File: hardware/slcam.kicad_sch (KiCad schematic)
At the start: 33 parts, among them J1 532610671, J2 Conn_01x08, J3 Conn_01x04, J4 532610371, J5 532610371, U1 STM32F103C8Tx, U2 W25Q128JVS, U3 TCAN330G, U4 TPS2044D, Y1 Crystal_GND24

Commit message: hardware: Minor improvements in the schematics #28
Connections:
- no-connect marks 23 -> 30
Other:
- note added: "Boot options: BOOT0=0 BOOT1=x - Main flash memory boot BOOT0=1 BOOT1=0 - System memory boot (bootloader) BOOT0=1 BOOT1=1 - RAM memory"
- note added: "I2C Pull-Up"
- note added: "J4 - PicoBlade CAN - 3 pins"
- note removed: "Boot options: BOOT0=0 BOOT1=x - main flash memory boot BOOT0=1 BOOT1=0 - system memory boot (boot loader) BOOT0=1 BOOT1=1 - RAM memory"
- note removed: "J4 - Pico Blade CAN - 3 pins"
- note removed: "i2c Pull-up"
- moved on the sheet: R4, R5, R6, R7

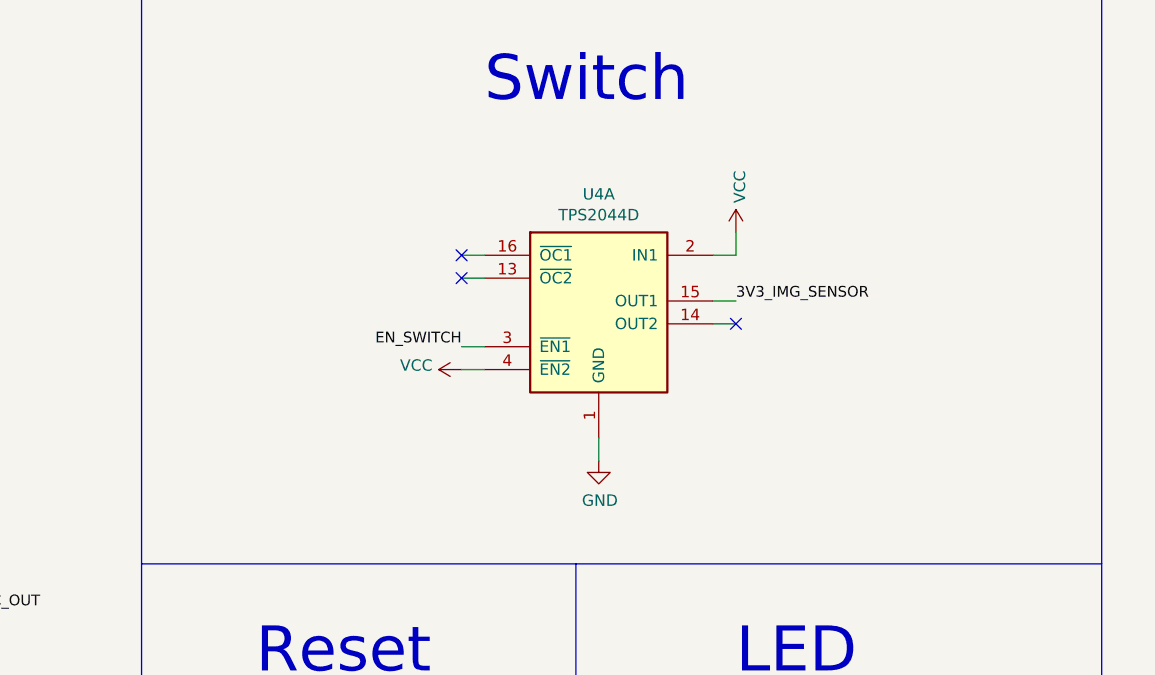
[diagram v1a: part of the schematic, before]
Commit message: hardware: Adding the second part of the TPS2044D IC #28
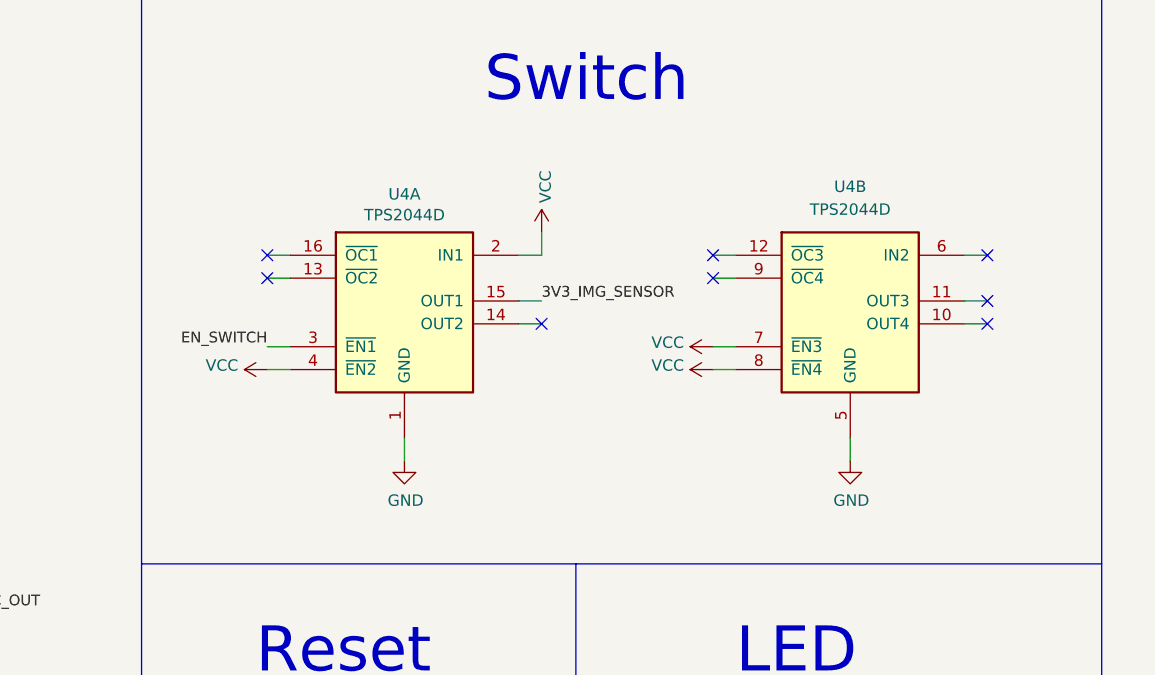
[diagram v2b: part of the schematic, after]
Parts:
- added unit 2 of U4
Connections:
- net GND: now also U4.5 (GND)
- net VCC: now also U4.7 (~{EN3}), U4.8 (~{EN4})
- no-connect marks 30 -> 35
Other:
- moved on the sheet: U4A

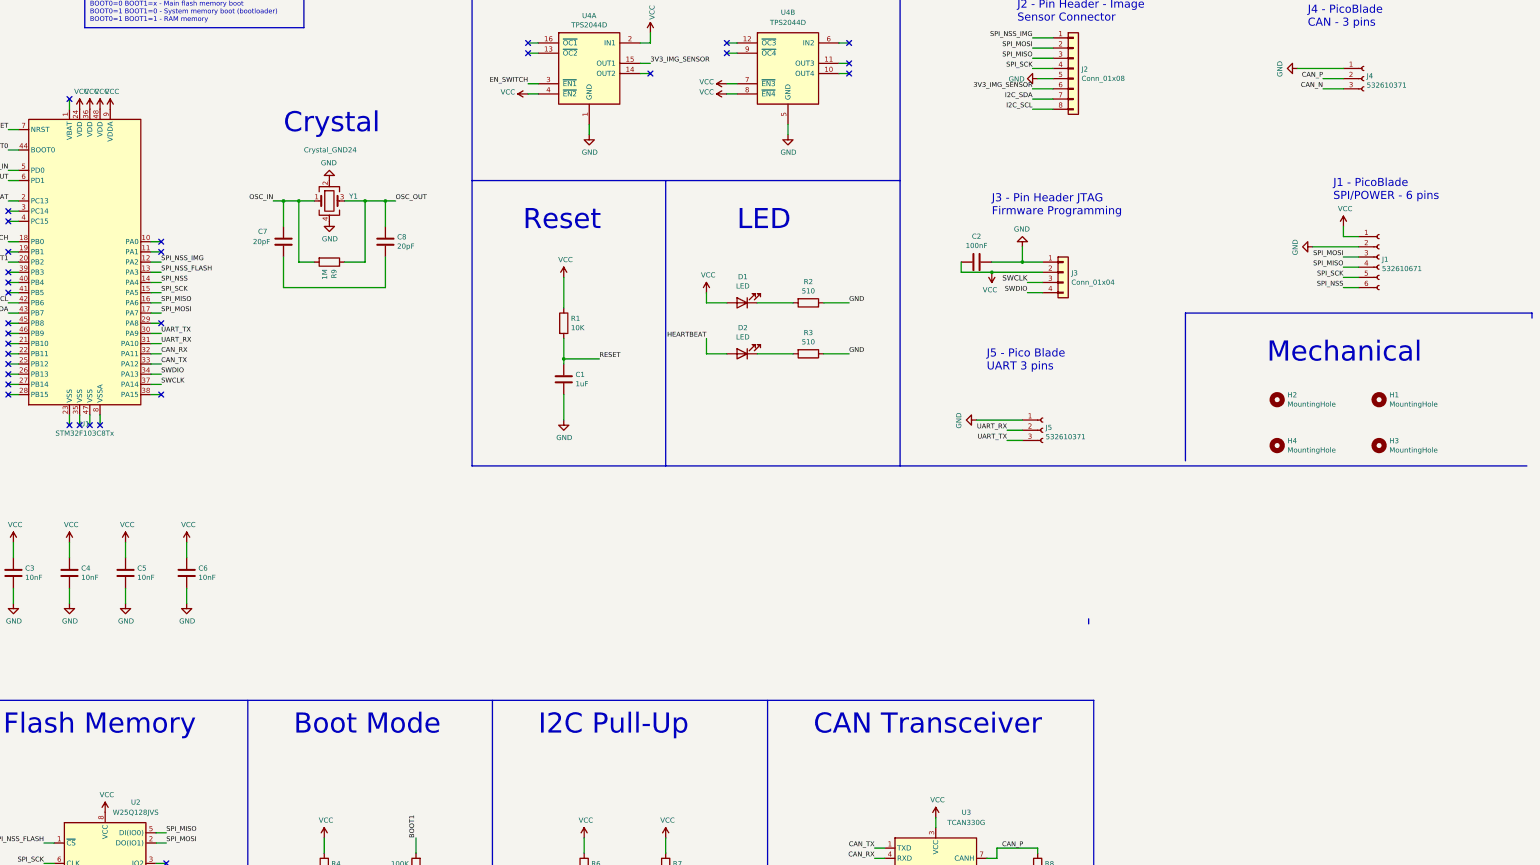
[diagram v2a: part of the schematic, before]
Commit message: hardware: Adding the PWR_FLAG to remove ERC errors #28
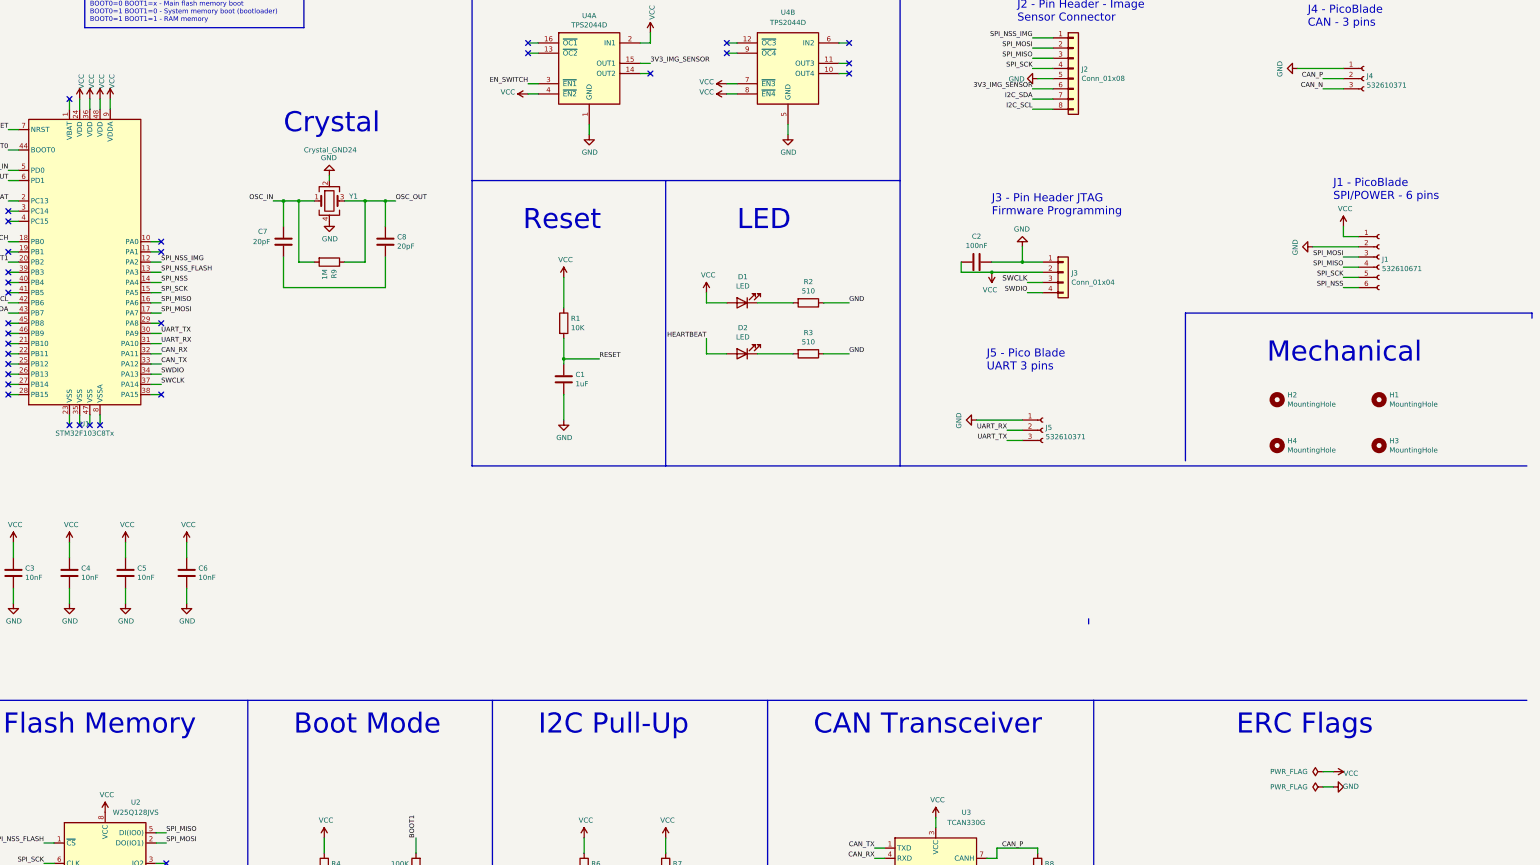
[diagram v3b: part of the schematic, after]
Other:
- note added: "ERC Flags"

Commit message: hardware: Updating the metadata of the schematics #28
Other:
- company: SpaceLab -> Space Technology Research Laboratory - SpaceLab
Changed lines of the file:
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@@
   (title_block
     (title "SLCam")
-    (date "2023-01-23")
+    (date "2023-02-07")
     (rev "v0.2")
-    (company "SpaceLab")
-    (comment 1 "Author: Vitória Beatriz Bianchin - Email: vitoriabbianchin@gmail.com")
+    (company "Space Technology Research Laboratory - SpaceLab")
+    (comment 1 "Support: Gabriel Mariano Marcelino <gabriel.mm8@gmail.com>")
+    (comment 2 "Author: Vitória Beatriz Bianchin <vitoriabbianchin@gmail.com>")
   )
   (junction (at 101.6 86.36) (diameter 0) (color 0 0 0 0)

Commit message: General fixes and improvements #45 #46 #47 #47 #48 #49 #50 #51
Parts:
- added C10, C9: 20pF, Capacitor_SMD:C_0603_1608Metric_Pad1.05x0.95mm_HandSolder, symbol Device:C
- added R10: 1M, Resistor_SMD:R_0603_1608Metric_Pad1.05x0.95mm_HandSolder, symbol Device:R
- added Y2: Crystal_GND24, Crystal:Crystal_SMD_ECS_CSM3X-2Pin_7.6x4.1mm, symbol Device:Crystal_GND24
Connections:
- net GND: now also U1.23 (VSS), U1.35 (VSS), U1.47 (VSS), U1.8 (VSSA), Y2.2, Y2.4
- net SPI_MISO: now also U2.2 (DO(IO1)); no longer J1.4 (Pin_4), U2.5 (DI(IO0))
- net SPI_MOSI: now also U2.5 (DI(IO0)); no longer J1.3 (Pin_3), U2.2 (DO(IO1))
- net SPI_SCK: no longer J1.5 (Pin_5)
- net SPI2_SCK: now reaches U1.26 (PB13)
- net SPI2_SCK: now also J1.5 (Pin_5)
- net SPI2_MISO: now reaches U1.27 (PB14)
- net SPI2_MISO: now also J1.3 (Pin_3)
- net SPI2_MOSI: now reaches U1.28 (PB15)
- net SPI2_MOSI: now also J1.4 (Pin_4)
- net OSC_IN2: now reaches U1.3 (PC14)
- net OSC_IN2: now also C9.1, R10.2, Y2.1
- net OSC_OUT2: now reaches U1.4 (PC15)
- net OSC_OUT2: now also C10.1, R10.1, Y2.3
- net CAN_SHDN: now reaches U1.40 (PB4)
- net CAN_SHDN: now also U3.5 (SHDN)
- net CAN_S: now reaches U1.41 (PB5)
- net CAN_S: now also U3.8 (S)
- net FLASH_WP: now reaches U1.45 (PB8)
- net FLASH_WP: now also U2.7 (IO3)
- net FLASH_HR: now reaches U1.46 (PB9)
- net FLASH_HR: now also U2.3 (IO2)
- net SPI_NSS renamed SPI2_NSS
- new net: C10.2, C9.2
- no-connect marks 35 -> 18
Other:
- note added: "SPI: Flash and Sensor SPI2: SPI/POWER Pico Blade Connector"

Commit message: hardware: fixing SPI pins #46
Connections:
- net SPI2_MISO: now also J2.3 (Pin_3), U2.2 (DO(IO1)); no longer J1.3 (Pin_3)
- net SPI2_MOSI: now also J2.2 (Pin_2), U2.5 (DI(IO0)); no longer J1.4 (Pin_4)
- net SPI2_SCK: now also J2.4 (Pin_4), U2.6 (CLK); no longer J1.5 (Pin_5)
- net SPI_MISO: now also J1.3 (Pin_3); no longer J2.3 (Pin_3), U2.2 (DO(IO1))
- net SPI_MOSI: now also J1.4 (Pin_4); no longer J2.2 (Pin_2), U2.5 (DI(IO0))
- net SPI_NSS_FLASH: now also U1.25 (PB12); no longer U1.13 (PA3)
- net SPI_SCK: now also J1.5 (Pin_5); no longer J2.4 (Pin_4), U2.6 (CLK)
- net SPI2_NSS renamed SPI_NSS
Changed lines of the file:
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@@
   (no_connect (at 29.21 124.46))
   (no_connect (at 208.28 49.53))
-  (no_connect (at 29.21 127))
+  (no_connect (at 67.31 104.14))
   (no_connect (at 67.31 134.62))
   (no_connect (at 67.31 116.84))
@@
     (effects (font (size 1.1938 1.1938)) (justify left bottom))
   )
-  (label "SPI2_MISO" (at 361.95 100.33 180)
+  (label "SPI_MISO" (at 361.95 100.33 180)
     (effects (font (size 1.1938 1.1938)) (justify right bottom))
   )
@@
     (effects (font (size 1.1938 1.1938)) (justify right bottom))
   )
-  (label "SPI_MISO" (at 284.48 50.8 180)
-    (effects (font (size 1.1938 1.1938)) (justify right bottom))
-  )
-  (label "SPI_MOSI" (at 284.48 48.26 180)
+  (label "SPI2_MISO" (at 284.48 50.8 180)
+    (effects (font (size 1.1938 1.1938)) (justify right bottom))
+  )
+  (label "SPI2_MOSI" (at 284.48 48.26 180)
     (effects (font (size 1.1938 1.1938)) (justify right bottom))
   )
@@
     (effects (font (size 1.1938 1.1938)) (justify right bottom))
   )
-  (label "SPI_SCK" (at 284.48 53.34 180)
+  (label "SPI2_SCK" (at 284.48 53.34 180)
     (effects (font (size 1.1938 1.1938)) (justify right bottom))
   )
@@
     (effects (font (size 1.1938 1.1938)) (justify right bottom))
   )
-  (label "SPI_NSS_FLASH" (at 67.31 104.14 0)
-    (effects (font (size 1.1938 1.1938)) (justify left bottom))
-  )
-  (label "SPI_SCK" (at 38.1 251.46 180)
+  (label "SPI2_SCK" (at 38.1 251.46 180)
     (effects (font (size 1.1938 1.1938)) (justify right bottom))
   )
@@
     (effects (font (size 1.1938 1.1938)) (justify right bottom))
   )
-  (label "SPI2_MOSI" (at 361.95 102.87 180)
+  (label "SPI_MOSI" (at 361.95 102.87 180)
     (effects (font (size 1.1938 1.1938)) (justify right bottom))
   )
@@
     (effects (font (size 1.1938 1.1938)) (justify right bottom))
   )
-  (label "SPI2_NSS" (at 67.31 106.68 0)
-    (effects (font (size 1.1938 1.1938)) (justify left bottom))
-  )
-  (label "SPI_MOSI" (at 68.58 243.84 0)
+  (label "SPI_NSS" (at 67.31 106.68 0)
+    (effects (font (size 1.1938 1.1938)) (justify left bottom))
+  )
+  (label "SPI2_MOSI" (at 68.58 243.84 0)
     (effects (font (size 1.1938 1.1938)) (justify left bottom))
   )
@@
     (effects (font (size 1.1938 1.1938)) (justify right bottom))
   )
-  (label "SPI2_NSS" (at 361.95 107.95 180)
+  (label "SPI_NSS" (at 361.95 107.95 180)
     (effects (font (size 1.1938 1.1938)) (justify right bottom))
   )
@@
     (effects (font (size 1.1938 1.1938)) (justify left bottom))
   )
-  (label "SPI2_SCK" (at 361.95 105.41 180)
+  (label "SPI_SCK" (at 361.95 105.41 180)
     (effects (font (size 1.1938 1.1938)) (justify right bottom))
   )
@@
     (effects (font (size 1.1938 1.1938)) (justify left bottom))
   )
+  (label "SPI_NSS_FLASH" (at 29.21 127 180)
+    (effects (font (size 1.1938 1.1938)) (justify right bottom))
+  )
   (label "SWCLK" (at 67.31 132.08 0)
     (effects (font (size 1.1938 1.1938)) (justify left bottom))
@@
     (effects (font (size 1.1938 1.1938)) (justify left bottom))
   )
-  (label "SPI_MISO" (at 68.58 246.38 0)
-    (effects (font (size 1.1938 1.1938)) (justify left bottom))
-  )
+  (label "SPI2_MISO" (at 68.58 246.38 0)
+    (effects (font (size 1.1938 1.1938)) (justify left bottom))
+  )

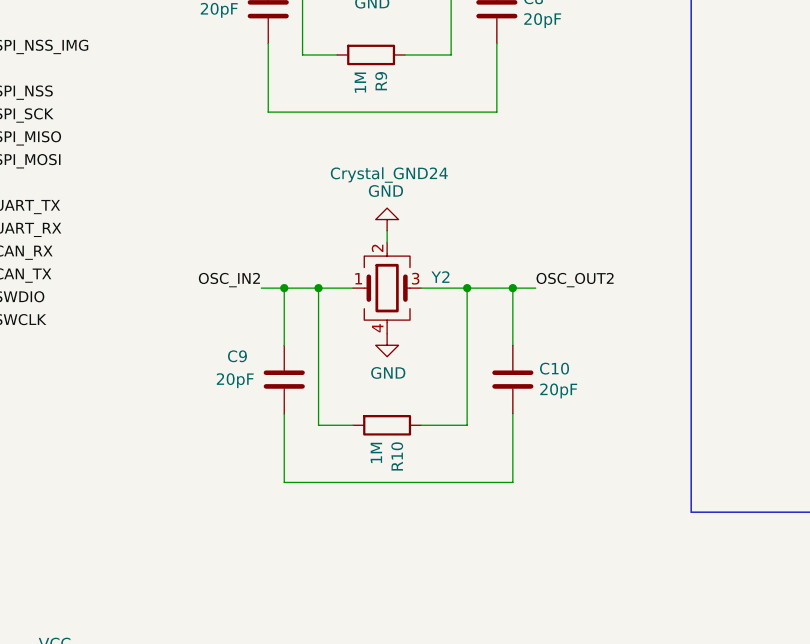
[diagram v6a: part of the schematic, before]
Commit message: hardware: fixing secong crystal schematics #45
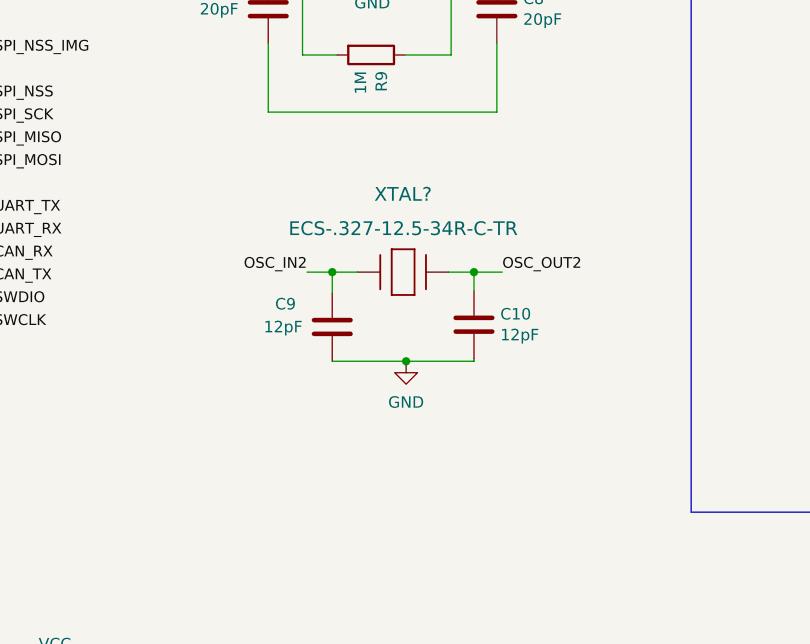
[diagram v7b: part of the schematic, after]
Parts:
- removed R10: 1M, Resistor_SMD:R_0603_1608Metric_Pad1.05x0.95mm_HandSolder, symbol Device:R
- removed Y2: Crystal_GND24, Crystal:Crystal_SMD_ECS_CSM3X-2Pin_7.6x4.1mm, symbol Device:Crystal_GND24
- added XTAL?: ECS-.327-12.5-34R-C-TR, XTAL_ECX-34R_ECS, symbol ECS-327-12-5-34R-C-TR:ECS-.327-12.5-34R-C-TR
- C10, C9: value 20pF -> 12pF
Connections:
- net GND: now also C10.2, C9.2
- net OSC_IN2: now also XTAL?.2
- net OSC_OUT2: now also XTAL?.1
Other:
- moved on the sheet: C10, C9
